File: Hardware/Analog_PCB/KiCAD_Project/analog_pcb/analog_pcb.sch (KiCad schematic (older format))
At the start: 36 parts, among them J1 Board to Board, U1 555, U2 LF356, U3 LTC1569-6

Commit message: Analog PCB Rev 1.0 complete.
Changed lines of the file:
@@
 Sheet 1 1
 Title "NSSL EFM Charge Amplifier"
-Date "2019-10-24"
+Date "2019-12-30"
 Rev "1.0"
 Comp "Leeman Geophysical LLC"
@@
 	1    0    0    -1
 $EndComp
+$Comp
+L power:+5V #PWR0101
+U 1 1 5E0B8B04
+P -1850 1975
+F 0 "#PWR0101" H -1850 1825 50  0001 C CNN
+F 1 "+5V" H -1835 2148 50  0000 C CNN
+F 2 "" H -1850 1975 50  0001 C CNN
+F 3 "" H -1850 1975 50  0001 C CNN
+	1    -1850 1975
+	0    1    1    0
+$EndComp
+$Comp
+L power:-5V #PWR0102
+U 1 1 5E0B8F15
+P -1850 2175
+F 0 "#PWR0102" H -1850 2275 50  0001 C CNN
+F 1 "-5V" H -1835 2348 50  0000 C CNN
+F 2 "" H -1850 2175 50  0001 C CNN
+F 3 "" H -1850 2175 50  0001 C CNN
+	1    -1850 2175
+	0    1    1    0
+$EndComp
+$Comp
+L power:GND #PWR0103
+U 1 1 5E0B92A7
+P -1850 2375
+F 0 "#PWR0103" H -1850 2125 50  0001 C CNN
+F 1 "GND" H -1845 2202 50  0000 C CNN
+F 2 "" H -1850 2375 50  0001 C CNN
+F 3 "" H -1850 2375 50  0001 C CNN
+	1    -1850 2375
+	0    -1   -1   0
+$EndComp
+$Comp
+L power:PWR_FLAG #FLG0101
+U 1 1 5E0B9584
+P -1850 1975
+F 0 "#FLG0101" H -1850 2050 50  0001 C CNN
+F 1 "PWR_FLAG" V -1850 2102 50  0000 L CNN
+F 2 "" H -1850 1975 50  0001 C CNN
+F 3 "~" H -1850 1975 50  0001 C CNN
+	1    -1850 1975
+	0    -1   -1   0
+$EndComp
+$Comp
+L power:PWR_FLAG #FLG0102
+U 1 1 5E0B9BD1
+P -1850 2175
+F 0 "#FLG0102" H -1850 2250 50  0001 C CNN
+F 1 "PWR_FLAG" V -1850 2302 50  0000 L CNN
+F 2 "" H -1850 2175 50  0001 C CNN
+F 3 "~" H -1850 2175 50  0001 C CNN
+	1    -1850 2175
+	0    -1   -1   0
+$EndComp
+$Comp
+L power:PWR_FLAG #FLG0103
+U 1 1 5E0B9D95
+P -1850 2375
+F 0 "#FLG0103" H -1850 2450 50  0001 C CNN
+F 1 "PWR_FLAG" V -1850 2502 50  0000 L CNN
+F 2 "" H -1850 2375 50  0001 C CNN
+F 3 "~" H -1850 2375 50  0001 C CNN
+	1    -1850 2375
+	0    -1   -1   0
+$EndComp
 $EndSCHEMATC

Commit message: Update schematic to use ATTINY for filter frequency generation.
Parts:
- removed C1, C4: 0.1u, Capacitors_SMD:C_0603_HandSoldering, symbol Device:C
- removed C2: 0.01u, Capacitors_SMD:C_0603_HandSoldering, symbol Device:C
- removed C3: 1u, Capacitors_SMD:C_0603_HandSoldering, symbol Device:C
- removed R1: 100, Resistors_SMD:R_0603_HandSoldering, symbol Device:R
- removed R2: 4.75k, Resistors_SMD:R_0603_HandSoldering, symbol Device:R
- removed U1: 555, Housings_SOIC:SOIC-8_3.9x4.9mm_Pitch1.27mm, symbol lib_sch:555
- added C?: 1u, Capacitors_SMD:C_0603_HandSoldering, symbol Device:C
- added C?: 0.1u, Capacitors_SMD:C_0603_HandSoldering, symbol Device:C
- added U?: ATtiny45-20SU, symbol MCU_Microchip_ATtiny:ATtiny45-20SU
- added Y?: 20MHz, symbol Device:Resonator
- C11: footprint Capacitors_SMD:C_1206_HandSoldering -> (none); Internal Part Number 1-0000420 -> 1-0000787
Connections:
- wire segments 103 -> 101
- no-connect marks 6 -> 9
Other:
- moved on the sheet: C10, C11, C12, C13, C14, C15, C16, C5, C6, C7, C8, C9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

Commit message: Revise analog PCB for Rev 2.0
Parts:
- removed Y?: 20MHz, symbol Device:Resonator
- added C13, C15: 20p, Capacitor_SMD:C_0603_1608Metric, symbol Device:C
- added PCB1: barepcb, symbol lib_sch:barepcb
- added Y1: 20MHz, Crystal:Crystal_HC49-U_Vertical, symbol Device:Crystal
- C1: renamed from C12; footprint Capacitors_SMD:C_0603_HandSoldering -> Capacitor_SMD:C_0603_1608Metric
- C10, C9: renamed from C?; footprint Capacitors_SMD:C_0603_HandSoldering -> Capacitor_SMD:C_0603_1608Metric
- C11: renamed from C7; footprint Capacitors_SMD:C_0603_HandSoldering -> Capacitor_SMD:C_0603_1608Metric
- C12: renamed from C8; footprint Capacitors_SMD:C_0603_HandSoldering -> Capacitor_SMD:C_0603_1608Metric
- C14: renamed from C9; footprint Capacitors_SMD:C_0603_HandSoldering -> Capacitor_SMD:C_0603_1608Metric
- C16: renamed from C10; footprint Capacitors_SMD:C_0603_HandSoldering -> Capacitor_SMD:C_0603_1608Metric
- C2: renamed from C15; footprint Capacitors_SMD:C_0603_HandSoldering -> Capacitor_SMD:C_0603_1608Metric
- C3: renamed from C13; footprint Capacitors_SMD:C_0603_HandSoldering -> Capacitor_SMD:C_0603_1608Metric
- C4: renamed from C16; footprint Capacitors_SMD:C_0603_HandSoldering -> Capacitor_SMD:C_0603_1608Metric
- C5: renamed from C14; footprint Capacitors_SMD:C_0603_HandSoldering -> Capacitor_SMD:C_0603_1608Metric
- C6: renamed from C11; footprint (none) -> lib_fp:1-0000787
- C7: renamed from C5; footprint Capacitors_SMD:C_0603_HandSoldering -> Capacitor_SMD:C_0603_1608Metric
- C8: renamed from C6; footprint Capacitors_SMD:C_0603_HandSoldering -> Capacitor_SMD:C_0603_1608Metric
- R2: renamed from R3; footprint Resistors_SMD:R_0603_HandSoldering -> Resistor_SMD:R_0603_1608Metric
- R3: renamed from R5; footprint Resistors_SMD:R_0603_HandSoldering -> Resistor_SMD:R_0603_1608Metric
- U3: renamed from U?; footprint (none) -> Package_SO:SOIC-8_3.9x4.9mm_P1.27mm
- renumbered R4 to R1, TP2 to TP1, TP3 to TP2, TP5 to TP3, TP1 to TP5, U2 to U1, U3 to U2
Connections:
- wire segments 101 -> 103

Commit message: Analog PCB hardware updates
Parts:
- J1: Internal Part Number 1-0000455 -> (none)
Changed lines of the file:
@@
 F 2 "Pin_Headers:Pin_Header_Straight_1x10_Pitch2.54mm" H 875 6450 50  0001 C CNN
 F 3 "~" H 875 6450 50  0001 C CNN
-F 4 "1-0000455" H 875 6450 50  0001 C CNN "Internal Part Number"
-F 5 "1" H 875 6450 50  0001 C CNN "Populated"
+F 4 "1" H 875 6450 50  0001 C CNN "Populated"
 	1    875  6450
 	-1   0    0    -1

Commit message: Get firmware up to current working state
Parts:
- U3: footprint Package_SO:SOIC-8_3.9x4.9mm_P1.27mm -> Package_SO:SOIC-8_5.275x5.275mm_P1.27mm
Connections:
- net FCLK: now also U3.5 (AREF/PB0); no longer U3.1 (~RESET~/PB5)
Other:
- moved on the sheet: TP5
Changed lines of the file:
@@
 Sheet 1 1
 Title "NSSL EFM Charge Amplifier"
-Date "2020-12-17"
-Rev "2.0"
+Date "2021-03-25"
+Rev "2.1"
 Comp "Leeman Geophysical LLC"
 Comment1 "(479) 373-3736"
@@
 Text GLabel 8325 3300 2    50   Output ~ 0
 Out
-Text GLabel 3600 7475 2    50   Output ~ 0
+Text GLabel 3725 6250 2    50   Output ~ 0
 FCLK
 Text GLabel 8275 3500 2    50   Input ~ 0
@@
 L Connector:TestPoint TP5
 U 1 1 5E07AFF7
-P 3525 7425
-F 0 "TP5" H 3475 7625 50  0000 L CNN
-F 1 "TestPoint" H 3583 7452 50  0001 L CNN
-F 2 "Measurement_Points:Measurement_Point_Round-SMD-Pad_Small" H 3725 7425 50  0001 C CNN
-F 3 "~" H 3725 7425 50  0001 C CNN
-F 4 "0-0000000" H 3525 7425 50  0001 C CNN "Internal Part Number"
-F 5 "0" H 3525 7425 50  0001 C CNN "Populated"
-	1    3525 7425
+P 3650 6200
+F 0 "TP5" H 3600 6400 50  0000 L CNN
+F 1 "TestPoint" H 3708 6227 50  0001 L CNN
+F 2 "Measurement_Points:Measurement_Point_Round-SMD-Pad_Small" H 3850 6200 50  0001 C CNN
+F 3 "~" H 3850 6200 50  0001 C CNN
+F 4 "0-0000000" H 3650 6200 50  0001 C CNN "Internal Part Number"
+F 5 "0" H 3650 6200 50  0001 C CNN "Populated"
+	1    3650 6200
 	1    0    0    -1
 $EndComp
@@
 F 0 "U3" H 2075 7300 50  0000 R CNN
 F 1 "ATtiny45-20SU" V 2175 7025 50  0000 R CNN
-F 2 "Package_SO:SOIC-8_3.9x4.9mm_P1.27mm" H 2500 6750 50  0001 C CIN
+F 2 "Package_SO:SOIC-8_5.275x5.275mm_P1.27mm" H 2500 6750 50  0001 C CIN
 F 3 "http://ww1.microchip.com/downloads/en/DeviceDoc/atmel-2586-avr-8-bit-microcontroller-attiny25-attiny45-attiny85_datasheet.pdf" H 2500 6750 50  0001 C CNN
 F 4 "1-0000758" H 2500 6750 50  0001 C CNN "Internal Part Number"
@@
 $EndComp
 Wire Wire Line
-	3100 6950 3275 6950
+	3400 6250 3650 6250
 Wire Wire Line
-	3275 6950 3275 7475
+	3650 6200 3650 6250
+Connection ~ 3650 6250
 Wire Wire Line
-	3275 7475 3525 7475
-Wire Wire Line
-	3525 7425 3525 7475
-Connection ~ 3525 7475
-Wire Wire Line
-	3525 7475 3600 7475
-NoConn ~ 3100 6450
+	3650 6250 3725 6250
 NoConn ~ 3100 6550
 NoConn ~ 3100 6650
@@
 	1    0    0    -1
 $EndComp
+NoConn ~ 3100 6950
+Wire Wire Line
+	3100 6450 3400 6450
+Wire Wire Line
+	3400 6450 3400 6250
 $EndSCHEMATC

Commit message: Fix footprint for ATTINY
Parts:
- PCB1: footprint (none) -> misc:barepcb
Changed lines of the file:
@@
 F 0 "PCB1" H 10753 6346 50  0000 L CNN
 F 1 "barepcb" H 10375 6300 50  0000 L CNN
-F 2 "" H 10525 6300 50  0001 C CNN
+F 2 "misc:barepcb" H 10525 6300 50  0001 C CNN
 F 3 "" H 10525 6300 50  0001 C CNN
 F 4 "3-0000066" H 10525 6300 50  0001 C CNN "Internal Part Number"

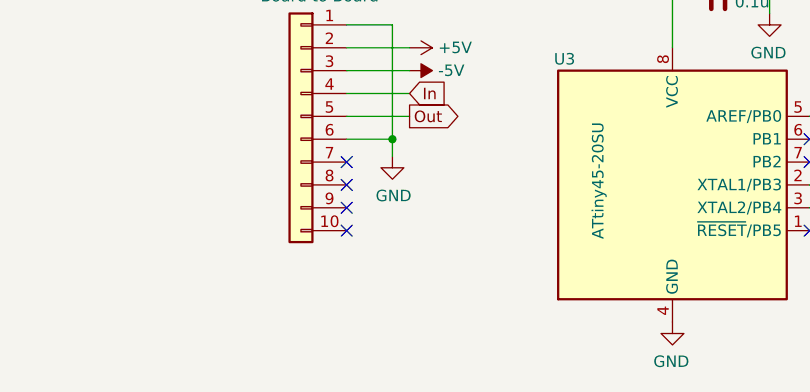
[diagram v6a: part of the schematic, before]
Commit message: Change PN for header to plug into analog PCBA.
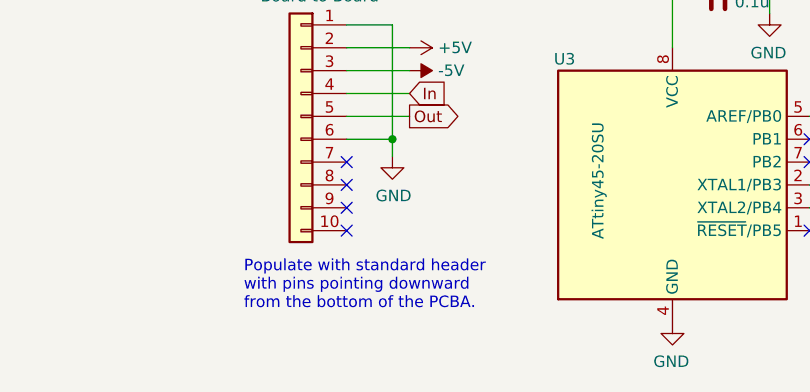
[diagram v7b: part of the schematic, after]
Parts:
- J1: Internal Part Number (none) -> 0-0000000
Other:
- note added: "Populate with standard header\nwith pins pointing downward\nfrom the bottom of the PCBA."
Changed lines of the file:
@@
 F 3 "~" H 875 6450 50  0001 C CNN
 F 4 "1" H 875 6450 50  0001 C CNN "Populated"
+F 5 "0-0000000" H 875 6450 50  0001 C CNN "Internal Part Number"
 	1    875  6450
 	-1   0    0    -1
@@
 Wire Wire Line
 	3400 6450 3400 6250
+Text Notes 625  7300 0    50   ~ 0
+Populate with standard header\nwith pins pointing downward\nfrom the bottom of the PCBA.
 $EndSCHEMATC

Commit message: Add Analog PCB REV 2.1 files
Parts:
- PCB1: Internal Part Number 3-0000066 -> 3-0000081
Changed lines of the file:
@@
 F 2 "misc:barepcb" H 10525 6300 50  0001 C CNN
 F 3 "" H 10525 6300 50  0001 C CNN
-F 4 "3-0000066" H 10525 6300 50  0001 C CNN "Internal Part Number"
+F 4 "3-0000081" H 10525 6300 50  0001 C CNN "Internal Part Number"
 F 5 "1" H 10525 6300 50  0001 C CNN "Populated"
 	1    10525 6300
